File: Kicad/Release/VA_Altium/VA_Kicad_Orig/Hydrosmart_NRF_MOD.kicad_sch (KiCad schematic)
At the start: 15 parts, among them J1 TC2030-IDC-NL, M1 AN54L15Q-U, U2 122, U5 112TR, Y1 FC-135_32.7680KA-AG5

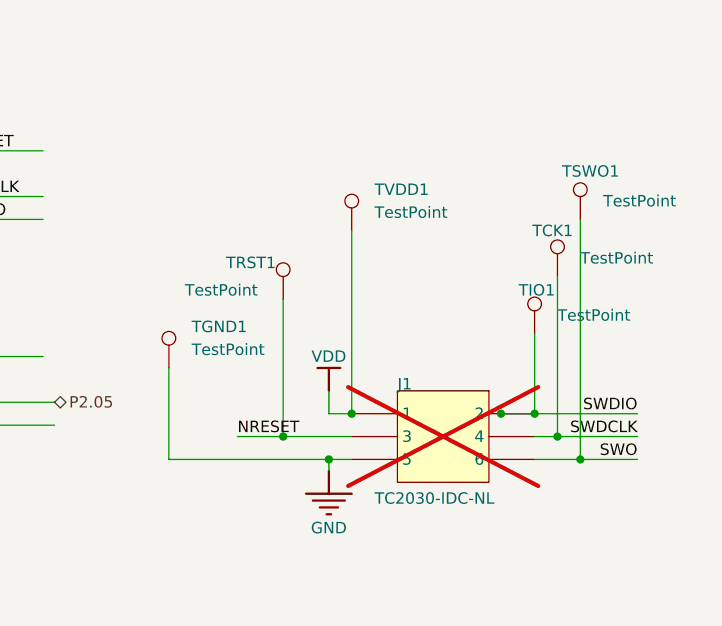
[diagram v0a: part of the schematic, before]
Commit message: VB changes start. Updated regulator and added test points
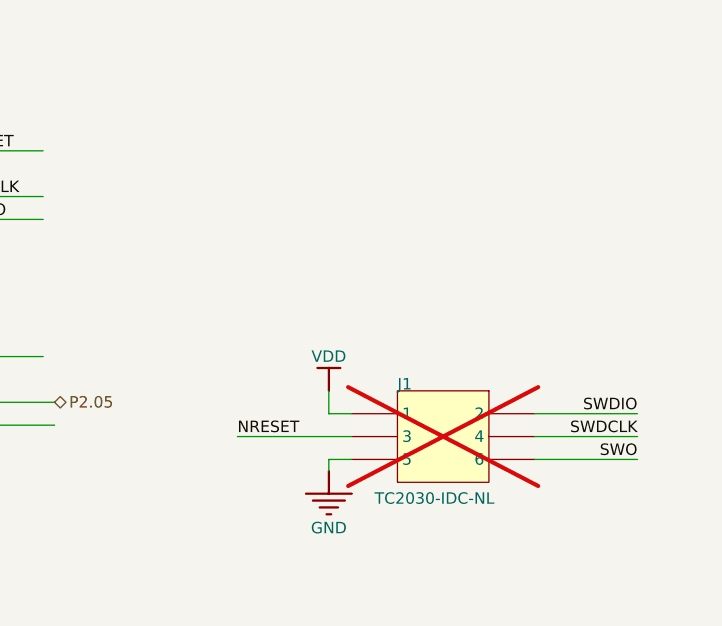
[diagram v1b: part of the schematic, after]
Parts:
- removed TCK1, TGND1, TIO1, TRST1, TSWO1, TVDD1: TestPoint, TestPoint:TestPoint_Pad_D1.0mm, symbol Connector:TestPoint
